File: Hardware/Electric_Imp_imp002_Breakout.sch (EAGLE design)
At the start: 2 parts

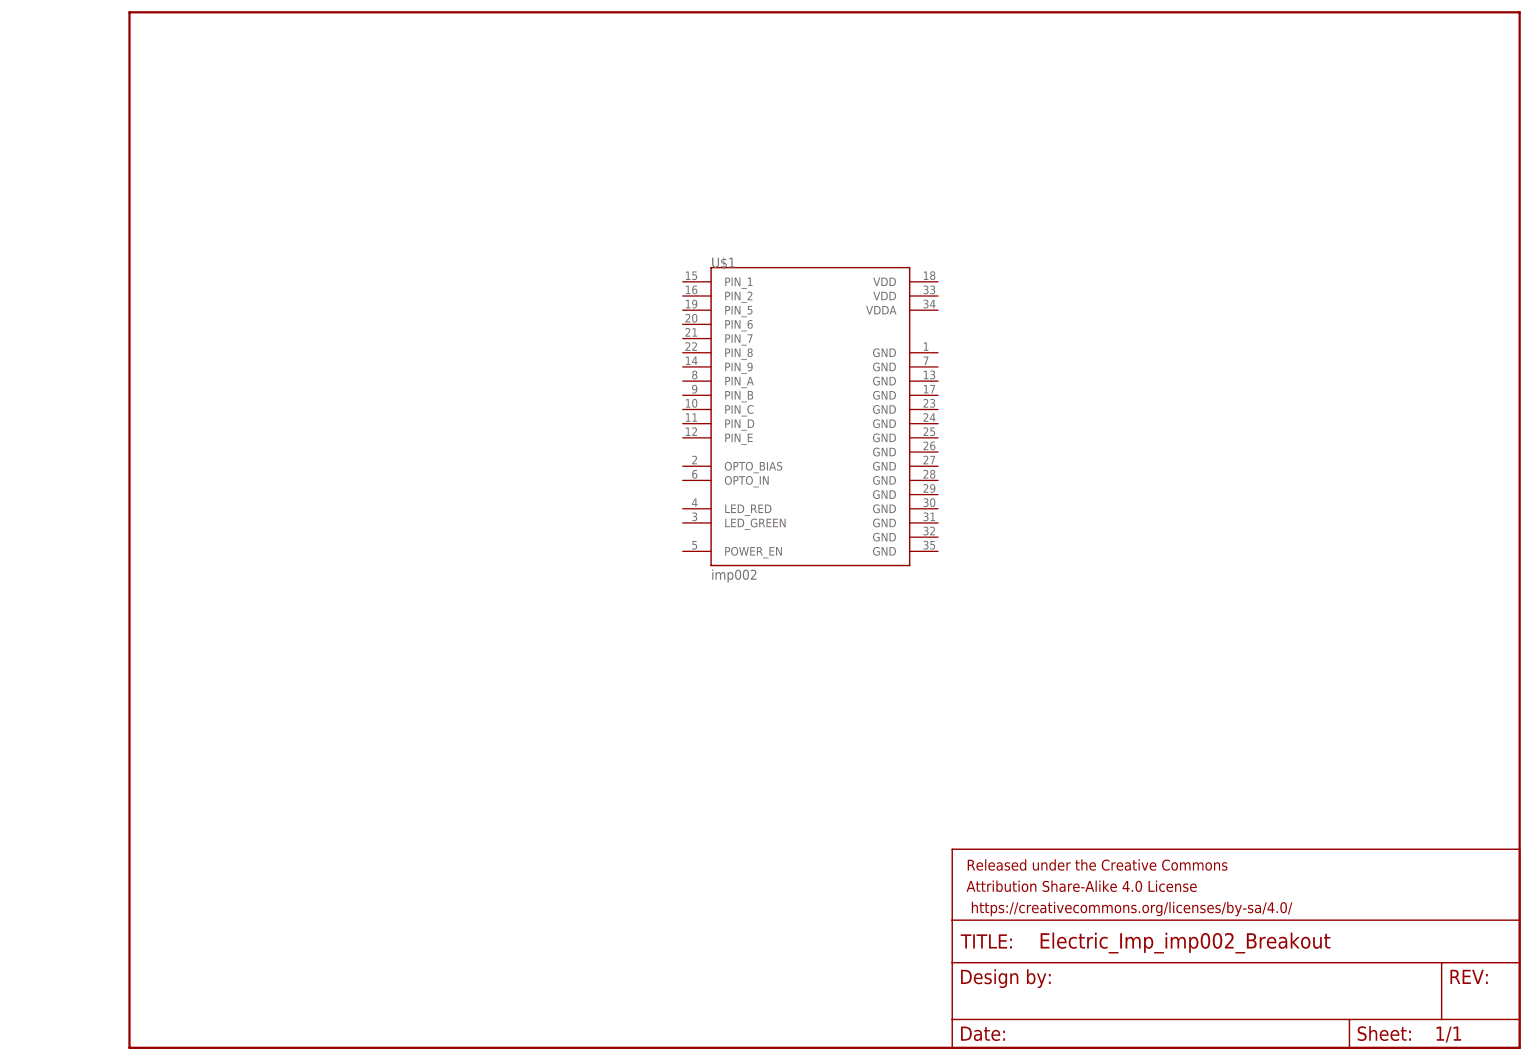
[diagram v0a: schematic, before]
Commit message: Created initial schematic and part placement
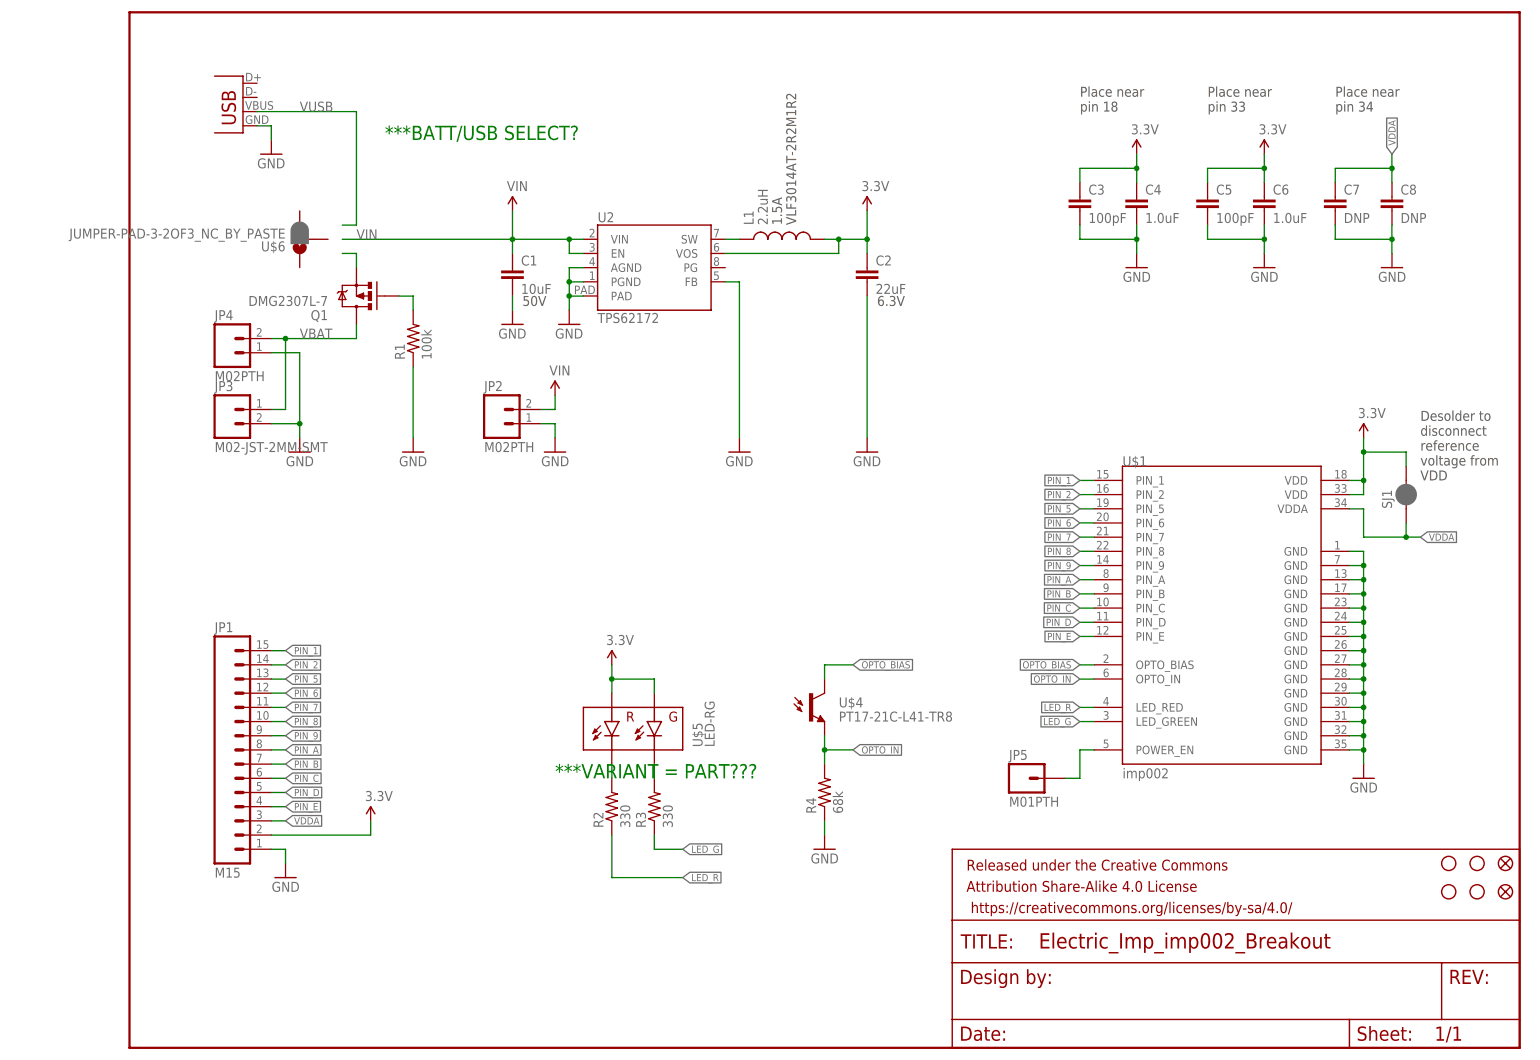
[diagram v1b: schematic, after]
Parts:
- added C1: 10uF, SparkFun-Passives:CAP1210
- added C2: 22uF, SparkFun-Passives:CAP0805
- added C3, C5: 100pF, SparkFun-Capacitors:CAP0603-CAP
- added C4, C6: 1.0uF, SparkFun-Capacitors:1.0UF-16V-10%(0603)
- added C7, C8: DNP, SparkFun-Capacitors:CAP0603-CAP
- added FID1, FID2: FIDUCIAL1X2, SparkFun-Aesthetics:FIDUCIAL1X2
- added JP1: M15, SparkFun-Connectors:M15
- added JP2, JP4: M02PTH, SparkFun-Connectors:M02PTH
- added JP3: M02-JST-2MM-SMT, SparkFun-Connectors:M02-JST-2MM-SMT
- added JP5: M01PTH, SparkFun-Connectors:M01PTH
- added L1: 2.2uH, SparkFun-Passives:INDUCTORVLF4012A
- added Q1: DMG2307L-7, SparkFun-DiscreteSemi:MOSFET-PCHANNELSMD
- added R1: 100k, SparkFun-Resistors:100KOHM1/10W1%(0603)
- added R2, R3: 330, SparkFun-Resistors:330OHM1/10W1%(0603)
- added R4: 68k, SparkFun-Resistors:RESISTOR0603
- added SJ1: JUMPER-PAD-2-NC_BY_PASTE, SparkFun-Passives:JUMPER-PAD-2-NC_BY_PASTE
- added STANDOFF1, STANDOFF2, STANDOFF3, STANDOFF4: STAND-OFF, SparkFun-Electromechanical:STAND-OFF
- added U$4: PT17-21C-L41-TR8, Testing:PT17-21C-L41-TR8
- added U$5: LED-RG, SparkFun-LED:LED-RG
- added U$6: JUMPER-PAD-3-2OF3_NC_BY_PASTE, SparkFun-Passives:JUMPER-PAD-3-2OF3_NC_BY_PASTE
- added U2: TPS62172, SparkFun-PowerIC:TPS62172
- added X1: USBSMD, SparkFun-Connectors:USBSMD
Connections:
- new net 3.3V: C2.1, C3.1, C4.1, C5.1, C6.1, JP1.2, L1.2, SJ1.2, U$1.VDD@18, U$1.VDD@33, U$5.GA, U$5.RA, U2.VOS
- new net GND: C1.2, C2.2, C3.2, C4.2, C5.2, C6.2, C7.2, C8.2, JP1.1, JP2.1, JP3.1, JP4.1, R1.1, R4.1, U$1.GND@1, U$1.GND@13, U$1.GND@17, U$1.GND@23, U$1.GND@24, U$1.GND@25, U$1.GND@26, U$1.GND@27, U$1.GND@28, U$1.GND@29, U$1.GND@30, U$1.GND@31, U$1.GND@32, U$1.GND@35, U$1.GND@7, U2.AGND, U2.FB, U2.PAD, U2.PGND, X1.GND
- new net LED_G: R3.1, U$1.LED_GREEN
- new net LED_R: R2.1, U$1.LED_RED
- new net N$1: L1.1, U2.SW
- new net N$2: Q1.G, R1.2
- new net N$3: JP5.1, U$1.POWER_EN
- new net N$4: R2.2, U$5.RC
- new net N$5: R3.2, U$5.GC
- new net N$6: Q1.S
- new net OPTO_BIAS: U$1.OPTO_BIAS, U$4.C
- new net OPTO_IN: R4.2, U$1.OPTO_IN, U$4.E
- new net PIN_1: JP1.15, U$1.PIN_1
- new net PIN_2: JP1.14, U$1.PIN_2
- new net PIN_5: JP1.13, U$1.PIN_5
- new net PIN_6: JP1.12, U$1.PIN_6
- new net PIN_7: JP1.11, U$1.PIN_7
- new net PIN_8: JP1.10, U$1.PIN_8
- new net PIN_9: JP1.9, U$1.PIN_9
- new net PIN_A: JP1.8, U$1.PIN_A
- new net PIN_B: JP1.7, U$1.PIN_B
- new net PIN_C: JP1.6, U$1.PIN_C
- new net PIN_D: JP1.5, U$1.PIN_D
- new net PIN_E: JP1.4, U$1.PIN_E
- new net VBAT: JP3.2, JP4.2, Q1.D
- new net VDDA: C7.1, C8.1, JP1.3, SJ1.1, U$1.VDDA
- new net VIN: C1.1, JP2.2, U2.EN, U2.VIN
- new net VUSB: X1.VBUS
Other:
- note added: "***BATT/USB SELECT?"
- note added: "***VARIANT = PART???"
- note added: "1.5A"
- note added: "50V"
- note added: "6.3V"
- note added: "Desolder to disconnect reference voltage from VDD"
- note added: "Place near pin 18"
- note added: "Place near pin 33"
- note added: "Place near pin 34"
- note added: "VLF3014AT-2R2M1R2"
- moved on the sheet: U$1

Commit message: Added automatic voltage source selector and battery level monitor in schematic
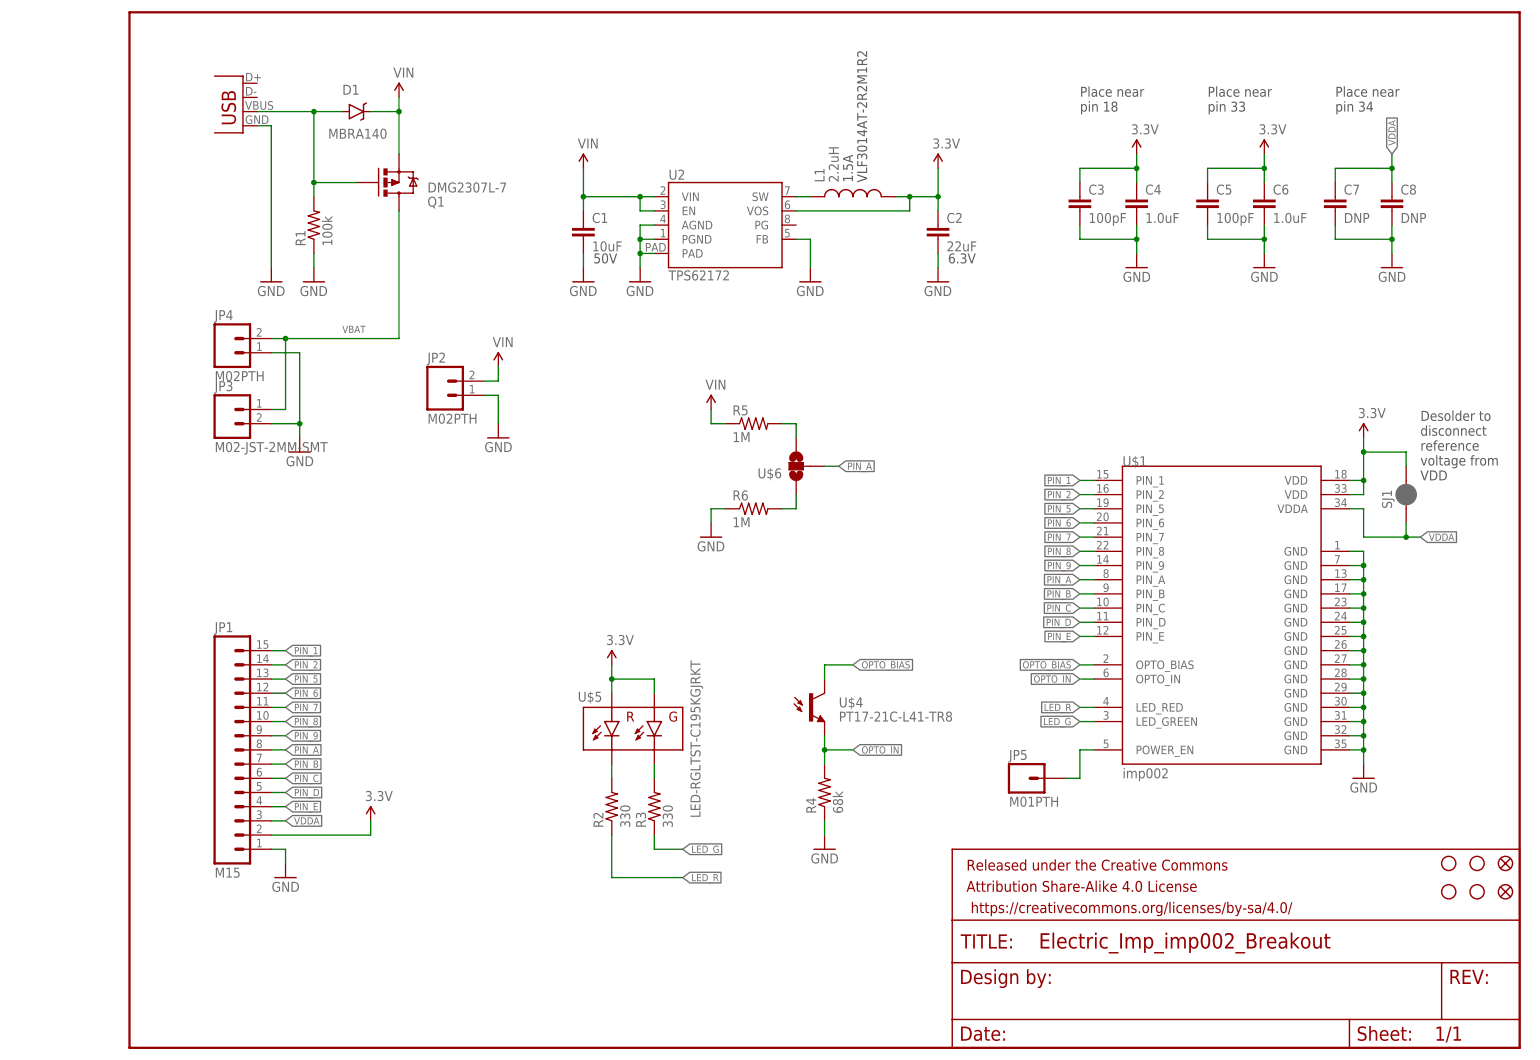
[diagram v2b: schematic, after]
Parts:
- added D1: MBRA140, SparkFun-DiscreteSemi:DIODE-SCHOTTKY-MBRA140
- added R5, R6: 1M, SparkFun-Resistors:1MOHM1/10W1%(0603)
- U$5: value LED-RG -> LED-RGLTST-C195KGJRKT; device SparkFun-LED:LED-RG -> SparkFun-LED:LED-RGLTST-C195KGJRKT
- U$6: value JUMPER-PAD-3-2OF3_NC_BY_PASTE -> JUMPER-PAD-3-NOFULL_BOX_SILK; device SparkFun-Passives:JUMPER-PAD-3-2OF3_NC_BY_PASTE -> SparkFun-Passives:JUMPER-PAD-3-NOFULL_BOX_SILK
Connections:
- removed net VUSB: X1.VBUS
- new net N$7: R6.2, U$6.1
- net GND: now also R6.1
- net N$2: now also D1.A, X1.VBUS
- net N$6: now also R5.2, U$6.3; no longer Q1.S
- net PIN_A: now also U$6.2
- net VIN: now also D1.C, Q1.S, R5.1
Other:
- note removed: "***BATT/USB SELECT?"
- note removed: "***VARIANT = PART???"
- moved on the sheet: C1, C2, JP2, L1, Q1, R1, U2

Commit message: Finished v01 prototype for review
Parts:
- added LOGO1: OSHW-LOGOS, SparkFun-Aesthetics:OSHW-LOGOS
- added LOGO2: SFE_LOGO_FLAME.1_INCH, SparkFun-Aesthetics:SFE_LOGO_FLAME.1_INCH
- added TP1, TP2: TEST-POINT3X5, SparkFun-Passives:TEST-POINT3X5
- added U$9: SFE_LOGO_NAME_WEB, SparkFun-Aesthetics:SFE_LOGO_NAME_WEB
- C7: value DNP -> 100pF
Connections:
- net N$3 renamed POWER_EN
- net GND: now also JP3.2; no longer JP3.1
- net OPTO_BIAS: now also TP1.1
- net OPTO_IN: now also TP2.1
- net PIN_1: now also JP1.10; no longer JP1.15
- net PIN_2: now also JP1.9; no longer JP1.14
- net PIN_5: now also JP1.8; no longer JP1.13
- net PIN_6: now also JP1.7; no longer JP1.12
- net PIN_7: now also JP1.6; no longer JP1.11
- net PIN_8: now also JP1.5; no longer JP1.10
- net PIN_9: now also JP1.4; no longer JP1.9
- net PIN_A: now also JP1.15; no longer JP1.8
- net PIN_B: now also JP1.14; no longer JP1.7
- net PIN_C: now also JP1.13; no longer JP1.6
- net PIN_D: now also JP1.12; no longer JP1.5
- net PIN_E: now also JP1.11; no longer JP1.4
- net VBAT: now also JP3.1; no longer JP3.2
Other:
- note added: "Battery Input"
- note added: "BlinkUp"
- note added: "By default, the jumper is open. Solder the entire jumper to allow for VIN measurements on the Imp."
- note added: "DC/DC Converter"
- note added: "Decoupling Capacitors"
- note added: "Desolder to disconnect analog reference voltage from VDD"
- note added: "Input Voltage Measurement"
- note added: "Input Voltage Source Selection"
- note added: "Pin Breakout"
- note added: "Shawn Hymel (SparkFun Electronics) Based on Electric Imp's Amber board"
- note added: "Status LEDs"
- note added: "imp002 Module"
- note added: "v01"
- note removed: "Desolder to disconnect reference voltage from VDD"
- moved on the sheet: JP1, JP3, JP5, R4, R5, R6, SJ1, U$1, U$6

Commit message: Made changes from review. Fixed VIn sense divider. Updated packages to remove $ symbols. Added +/- silk to battery. Added voltage input range text on sch and brd. Moved decoup caps on bottom of imp to remove loop.
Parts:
- removed U$4: PT17-21C-L41-TR8, Testing:PT17-21C-L41-TR8
- added Q2: PHOTOTRANSISTORPT17-21C-L41-TR8, SparkFun-DiscreteSemi:PHOTOTRANSISTORPT17-21C-L41-TR8
- R5: value 1M -> 33k; device SparkFun-Resistors:1MOHM1/10W1%(0603) -> SparkFun-Resistors:33KOHM1/10W1%(0603)
- R6: value 1M -> 62k; device SparkFun-Resistors:1MOHM1/10W1%(0603) -> SparkFun-Resistors:RESISTOR0603
- renumbered U$1 to U1, U$5 to D2
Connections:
- net OPTO_BIAS: now also Q2.C; no longer U$4.C
- net OPTO_IN: now also Q2.E; no longer U$4.E
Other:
- note added: "By default, the jumper is open. Solder the entire jumper to allow for VIN measurements on the Imp. This limits VIN to 5V max."
- note added: "VIN = 3.3 - 17V"
- note removed: "By default, the jumper is open. Solder the entire jumper to allow for VIN measurements on the Imp."

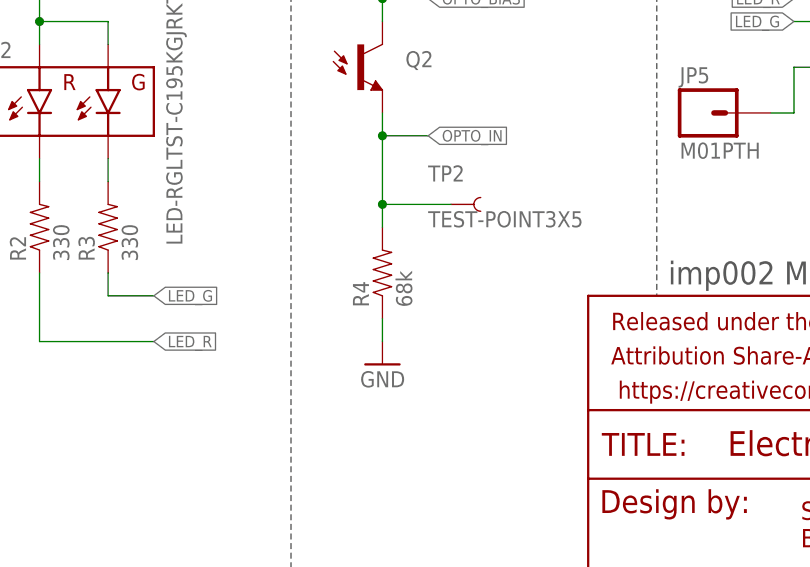
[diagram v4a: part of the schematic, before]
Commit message: Changed 68k resistor to 62k
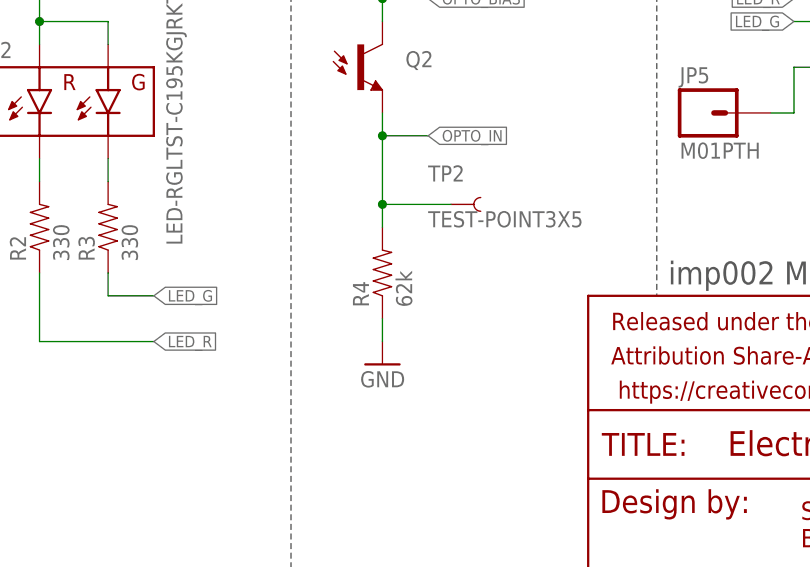
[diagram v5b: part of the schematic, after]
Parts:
- R4: value 68k -> 62k
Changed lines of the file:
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@@
 <setting verticaltext="up"/>
 </settings>
-<grid distance="0.1" unitdist="inch" unit="inch" style="lines" multiple="1" display="yes" altdistance="0.01" altunitdist="inch" altunit="inch"/>
+<grid distance="0.1" unitdist="inch" unit="inch" style="lines" multiple="1" display="no" altdistance="0.01" altunitdist="inch" altunit="inch"/>
 <layers>
 <layer number="1" name="Top" color="4" fill="1" visible="no" active="no"/>
@@
 <part name="R3" library="SparkFun-Resistors" deviceset="330OHM1/10W1%(0603)" device="" value="330"/>
 <part name="P+6" library="SparkFun-Aesthetics" deviceset="3.3V" device=""/>
-<part name="R4" library="SparkFun-Resistors" deviceset="RESISTOR" device="0603" value="68k"/>
+<part name="R4" library="SparkFun-Resistors" deviceset="RESISTOR" device="0603" value="62k"/>
 <part name="GND13" library="SparkFun-Aesthetics" deviceset="GND" device=""/>
 <part name="JP1" library="SparkFun-Connectors" deviceset="M15" device=""/>

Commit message: Added silk to the 3-way jumper, moved marking for dual-color diode to outside footprint, and changed phototransistor gain resistor to 33k
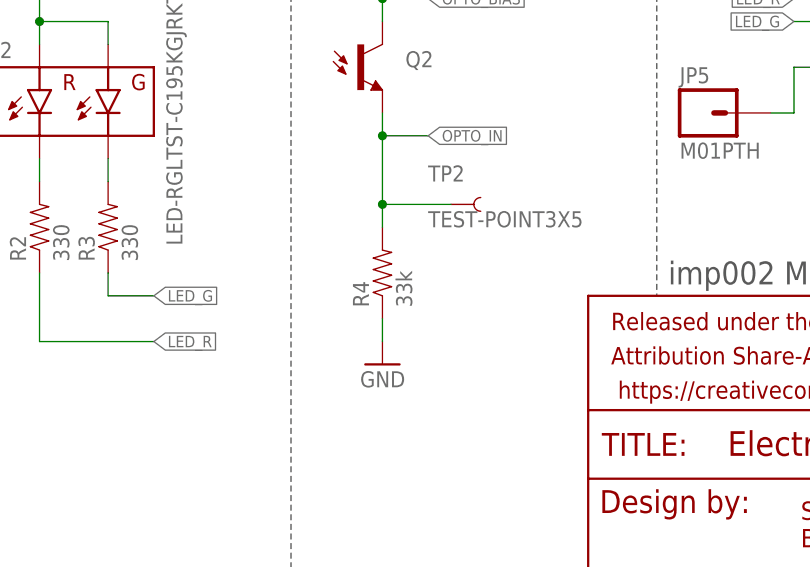
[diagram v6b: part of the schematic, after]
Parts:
- R4: value 62k -> 33k; device SparkFun-Resistors:RESISTOR0603 -> SparkFun-Resistors:33KOHM1/10W1%(0603)
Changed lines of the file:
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@@
 <part name="R3" library="SparkFun-Resistors" deviceset="330OHM1/10W1%(0603)" device="" value="330"/>
 <part name="P+6" library="SparkFun-Aesthetics" deviceset="3.3V" device=""/>
-<part name="R4" library="SparkFun-Resistors" deviceset="RESISTOR" device="0603" value="62k"/>
+<part name="R4" library="SparkFun-Resistors" deviceset="33KOHM1/10W1%(0603)" device="" value="33k"/>
 <part name="GND13" library="SparkFun-Aesthetics" deviceset="GND" device=""/>
 <part name="JP1" library="SparkFun-Connectors" deviceset="M15" device=""/>

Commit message: Changed rev number to v10
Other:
- note added: "v10"
- note removed: "v01"
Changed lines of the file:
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@@
 <text x="170.942" y="7.62" size="2.032" layer="94">Shawn Hymel (SparkFun Electronics)
 Based on Electric Imp's Amber board</text>
-<text x="238.76" y="7.62" size="2.54" layer="94">v01</text>
+<text x="238.76" y="7.62" size="2.54" layer="94">v10</text>
 <text x="48.26" y="99.06" size="1.778" layer="97">VIN = 3.3 - 17V</text>
 </plain>
